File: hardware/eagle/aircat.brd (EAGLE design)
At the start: 53.2 x 59.6 mm, 180 parts, among them CON1 A10_OLINUXINO_LIME_SHIELD_TEM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, CON2 ANALOG_OUT, CON3 ANALOG_IN, CON4 SPDIF_OUT, U1 PCM3168A, U2 OPA1644AIPW, U3 OPA1644AIPW, U4 OPA1644AIPW, U6 LM2662M

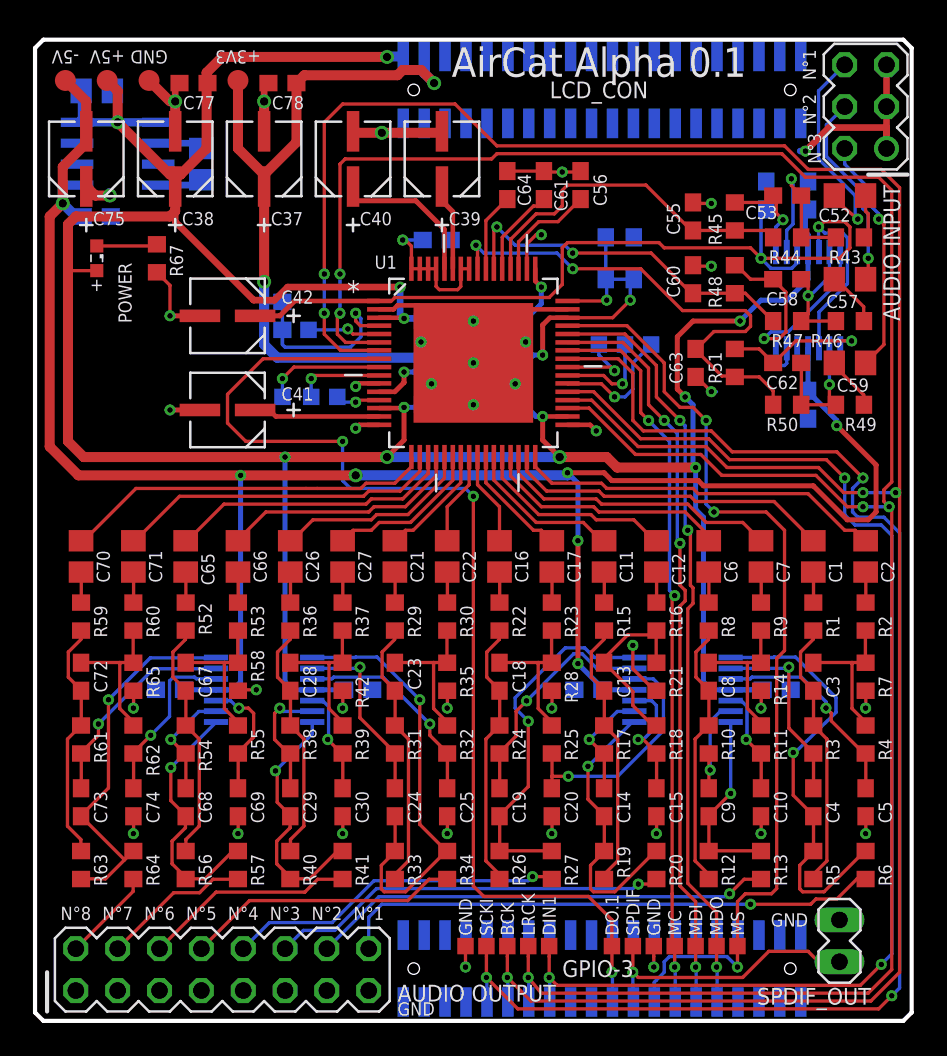
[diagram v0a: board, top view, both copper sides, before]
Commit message: added test points for unused data lines
fix #7
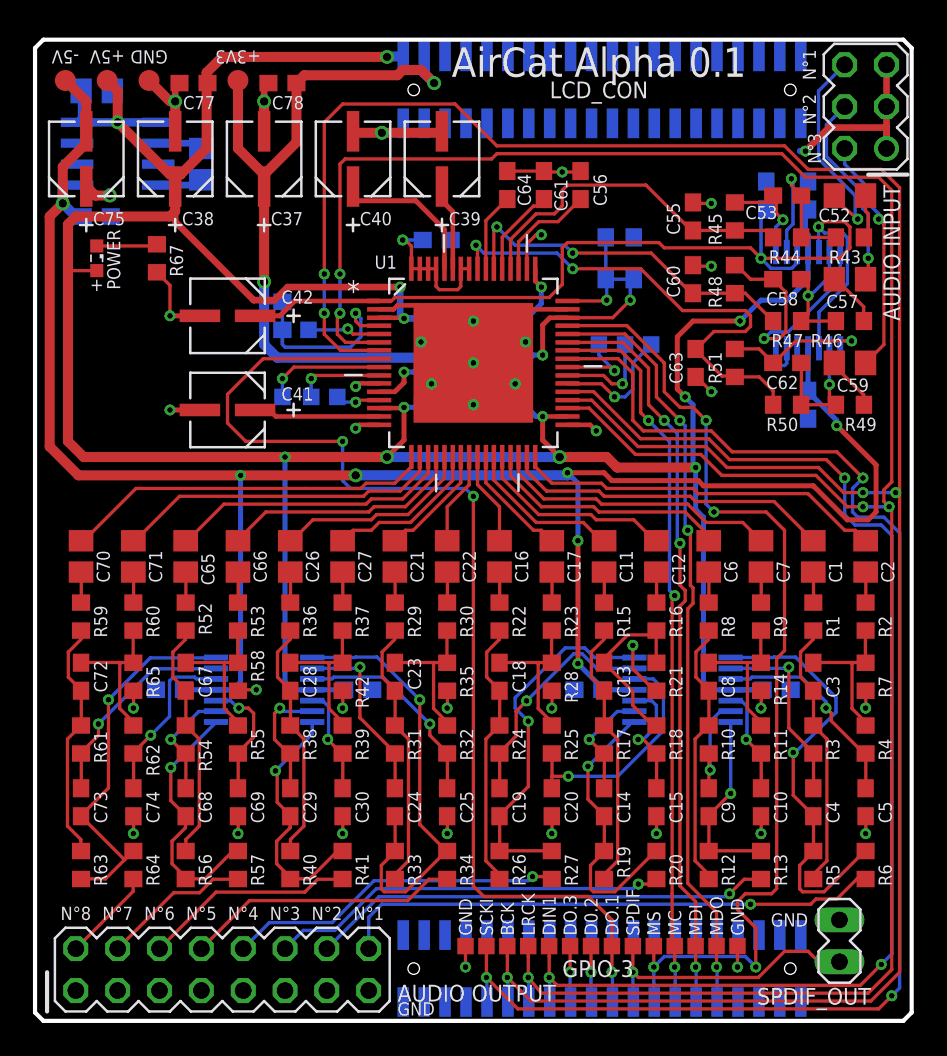
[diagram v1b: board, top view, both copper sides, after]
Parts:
- added DOUT2(NC), DOUT3(NC): TPTP10SQ, testpad:TP10SQ
- moved GND@2 5.08 mm to (16.0, -25.2)
- moved MS 5.08 mm to (11.0, -25.2)
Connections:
- new net DOUT2(NC): CON1.3-20, DOUT2(NC).TP
- new net DOUT3(NC): CON1.3-18, DOUT3(NC).TP
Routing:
- net DOUT2(NC): track 0.00 -> 3.43 mm, vias 0 -> 1
- net DOUT3(NC): track 0.00 -> 3.43 mm, vias 0 -> 1
- net MS: track 58.5 -> 61.6 mm, vias 3 -> 4
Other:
- board text added: "D0.2"
- board text added: "DO.3"

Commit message: minor electrical line path optimizations
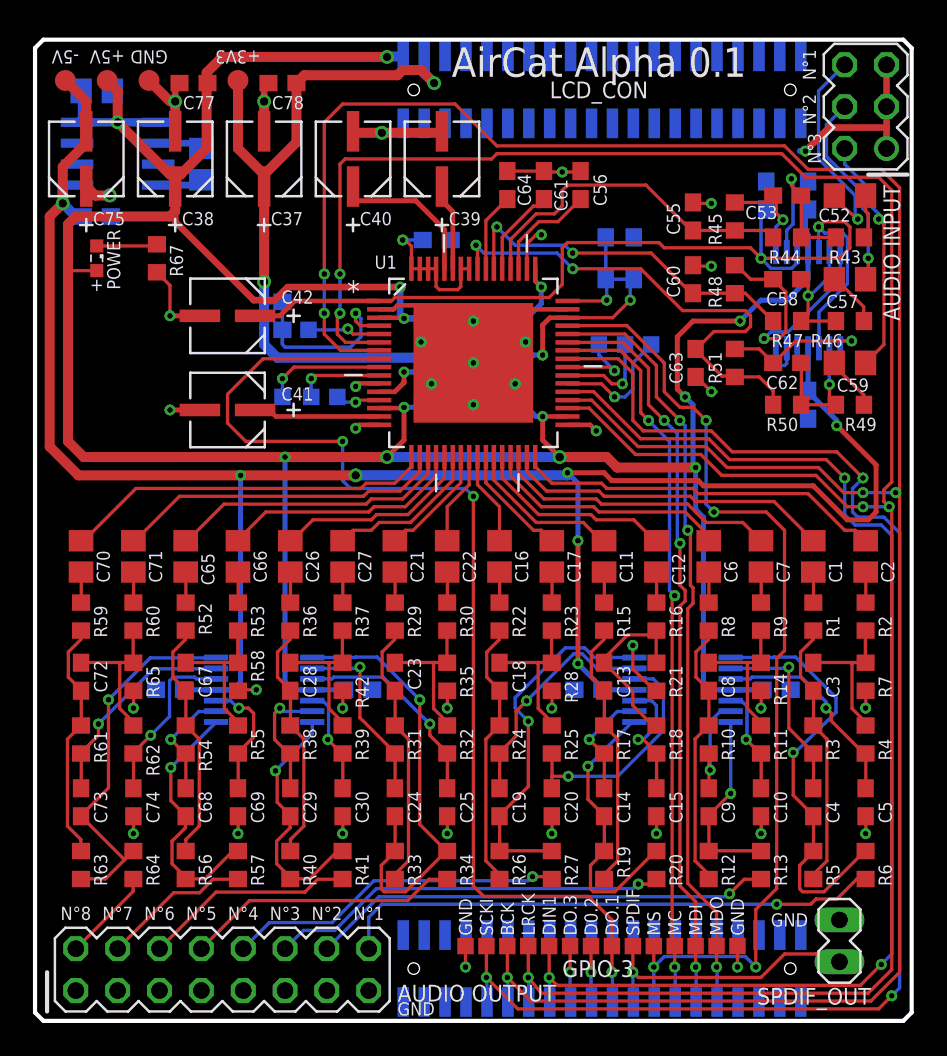
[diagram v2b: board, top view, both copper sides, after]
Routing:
- net MS: track 61.6 -> 59.7 mm
- net GND: track 82.3 -> 81.0 mm

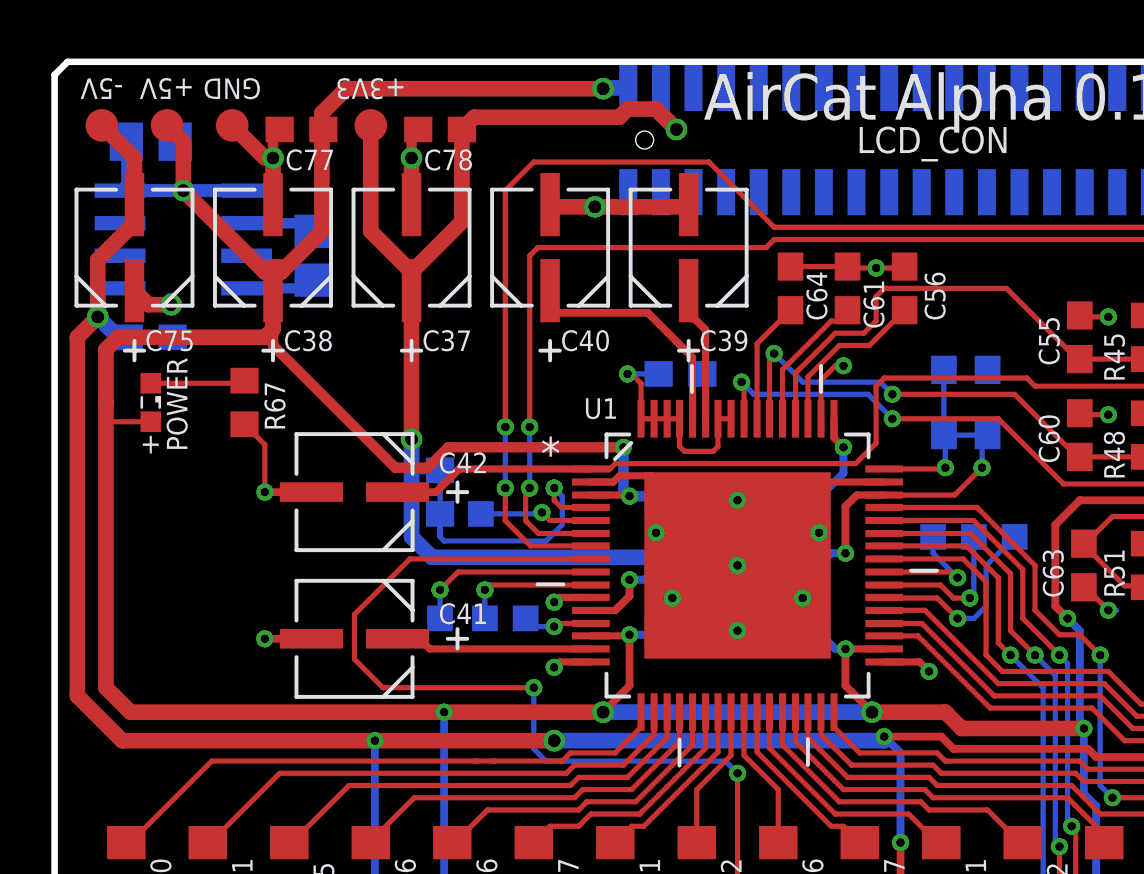
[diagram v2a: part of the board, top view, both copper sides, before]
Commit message: relocated componant laying around GPIO-4
fix #9
LM2662 and its capacitors having relocated in order not to enter in
contact with the GPIO-4 connector.
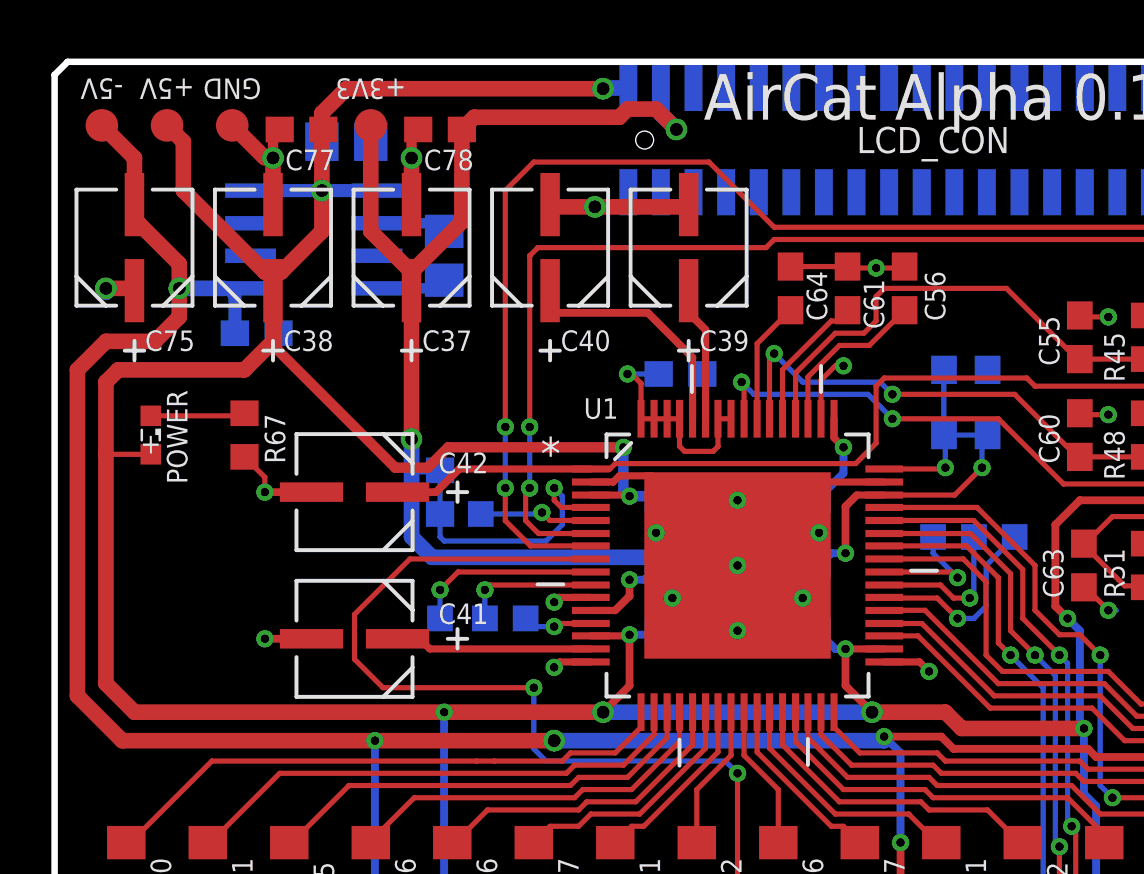
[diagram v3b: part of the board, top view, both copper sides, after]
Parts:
- moved C50 7.62 mm to (-15.2, 26.7)
- moved C49 5.08 mm to (-11.4, 22.2)
- moved U6 5.08 mm to (-16.5, 22.9)
- moved C48 4.13 mm to (-18.7, 19.2)
- moved POWER 1.27 mm to (-22.9, 15.2)
- moved R67 1.27 mm to (-19.2, 15.2)
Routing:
- net -5V: track 124.7 -> 127.4 mm
- net GND: track 81.0 -> 79.4 mm
- net +3V3: track 86.7 -> 85.8 mm

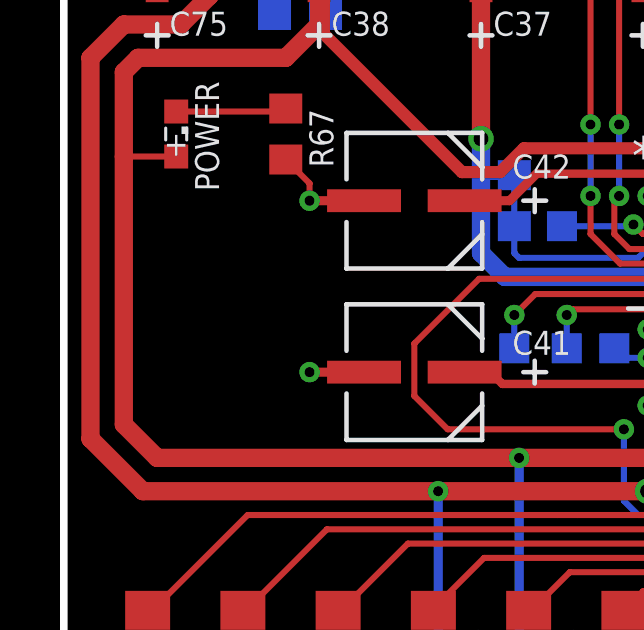
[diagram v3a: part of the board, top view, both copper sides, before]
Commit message: added licence logo
fix #6
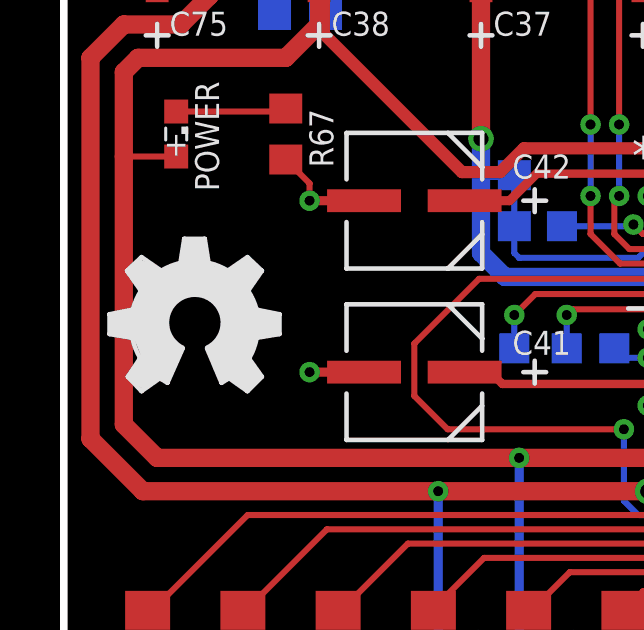
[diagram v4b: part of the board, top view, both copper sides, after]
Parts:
- added LOGO1: OSHW_LOGO_FILLX0200-NT, ohw-logo:OSHW_FILLX200_NOTEXT
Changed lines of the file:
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@@
 <layer number="25" name="tNames" color="7" fill="1" visible="yes" active="yes"/>
 <layer number="26" name="bNames" color="7" fill="1" visible="yes" active="yes"/>
-<layer number="27" name="tValues" color="7" fill="1" visible="yes" active="yes"/>
-<layer number="28" name="bValues" color="7" fill="1" visible="yes" active="yes"/>
+<layer number="27" name="tValues" color="7" fill="1" visible="no" active="yes"/>
+<layer number="28" name="bValues" color="7" fill="1" visible="no" active="yes"/>
 <layer number="29" name="tStop" color="7" fill="3" visible="no" active="yes"/>
 <layer number="30" name="bStop" color="7" fill="6" visible="no" active="yes"/>
@@
 <layer number="98" name="Guide" color="6" fill="1" visible="no" active="no"/>
 <layer number="100" name="Muster" color="7" fill="1" visible="no" active="no"/>
+<layer number="101" name="DRAWREF" color="11" fill="1" visible="no" active="yes"/>
+<layer number="102" name="Vscore" color="7" fill="1" visible="no" active="yes"/>
+<layer number="103" name="tMap" color="7" fill="1" visible="no" active="yes"/>
+<layer number="104" name="Name" color="16" fill="1" visible="no" active="yes"/>
+<layer number="105" name="tPlate" color="7" fill="1" visible="no" active="yes"/>
+<layer number="106" name="bPlate" color="7" fill="1" visible="no" active="yes"/>
+<layer number="107" name="Crop" color="7" fill="1" visible="no" active="yes"/>
+<layer number="116" name="Patch_BOT" color="9" fill="4" visible="no" active="yes"/>
+<layer number="121" name="_tsilk" color="7" fill="1" visible="no" active="yes"/>
+<layer number="122" name="_bsilk" color="7" fill="1" visible="no" active="yes"/>
+<layer number="144" name="DrillLegend" color="7" fill="1" visible="no" active="yes"/>
+<layer number="151" name="HeatSink" color="7" fill="1" visible="no" active="yes"/>
+<layer number="200" name="200bmp" color="1" fill="10" visible="no" active="yes"/>
+<layer number="201" name="201bmp" color="2" fill="10" visible="no" active="yes"/>
+<layer number="202" name="202bmp" color="3" fill="10" visible="no" active="yes"/>
+<layer number="203" name="203bmp" color="4" fill="10" visible="no" active="yes"/>
+<layer number="204" name="204bmp" color="5" fill="10" visible="no" active="yes"/>
+<layer number="205" name="205bmp" color="6" fill="10" visible="no" active="yes"/>
+<layer number="206" name="206bmp" color="7" fill="10" visible="no" active="yes"/>
+<layer number="207" name="207bmp" color="15" fill="10" visible="no" active="yes"/>
+<layer number="208" name="208bmp" color="9" fill="10" visible="no" active="yes"/>
+<layer number="209" name="209bmp" color="7" fill="1" visible="no" active="yes"/>
+<layer number="210" name="210bmp" color="7" fill="1" visible="no" active="yes"/>
+<layer number="211" name="211bmp" color="7" fill="1" visible="no" active="yes"/>
+<layer number="212" name="212bmp" color="7" fill="1" visible="no" active="yes"/>
+<layer number="213" name="213bmp" color="7" fill="1" visible="no" active="yes"/>
+<layer number="214" name="214bmp" color="7" fill="1" visible="no" active="yes"/>
+<layer number="215" name="215bmp" color="7" fill="1" visible="no" active="yes"/>
+<layer number="216" name="216bmp" color="7" fill="1" visible="no" active="yes"/>
 <layer number="250" name="Descript" color="3" fill="1" visible="no" active="no"/>
 <layer number="251" name="SMDround" color="12" fill="11" visible="no" active="no"/>
+<layer number="254" name="cooling" color="7" fill="1" visible="no" active="yes"/>
 </layers>
 <board>
@@
 <attribute name="TP_SIGNAL_NAME" value="" x="5.87375" y="-27.14625" size="1" layer="37"/>
 </element>
+<element name="LOGO1" library="ohw-logo" package="OSHW_FILLX200_NOTEXT" value="OSHW_LOGO_FILLX0200-NT" x="-25.0825" y="6.6675"/>
 </elements>
 <signals>
@@
 </signal>
 </signals>
-<errors>
-</errors>
 </board>
 </drawing>
